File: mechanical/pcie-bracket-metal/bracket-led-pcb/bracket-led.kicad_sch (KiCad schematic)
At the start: 5 parts, among them J1 SM08B-SURS-TF(LF)(SN)

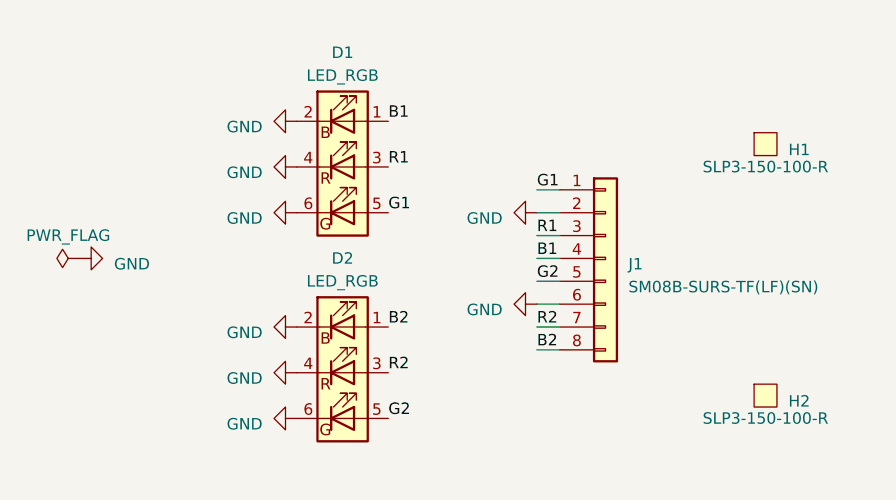
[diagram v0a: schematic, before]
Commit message: Update LED panel design after review
- Reduce size to fit in current allowed volume
- Move connector for improved strain relief
- Match RGB pinout on fmc host
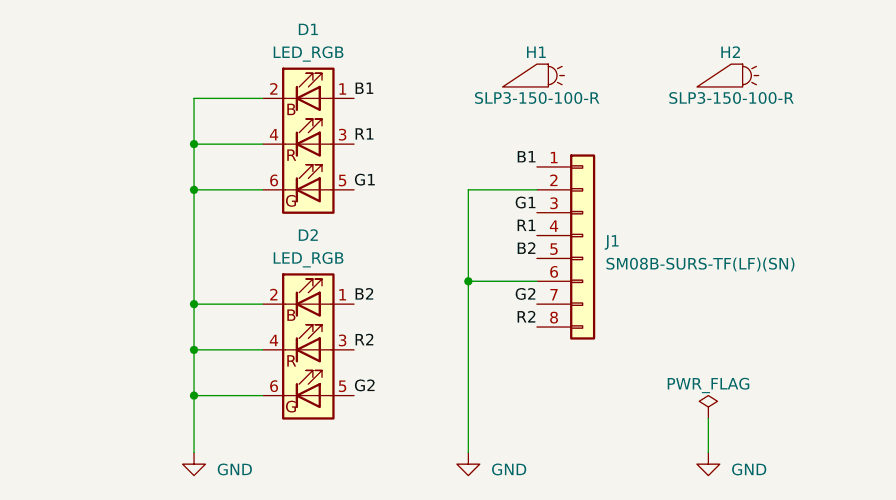
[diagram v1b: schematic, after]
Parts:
- H1: renamed from H2; symbol Open Ephys:SLP3-150-100-R -> jonnew:LIGHTPIPE
- H2: renamed from H1; symbol Open Ephys:SLP3-150-100-R -> jonnew:LIGHTPIPE
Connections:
- net B1: now also J1.1 (Pin_1); no longer J1.4 (Pin_4)
- net B2: now also J1.5 (Pin_5); no longer J1.8 (Pin_8)
- net G1: now also J1.3 (Pin_3); no longer J1.1 (Pin_1)
- net G2: now also J1.7 (Pin_7); no longer J1.5 (Pin_5)
- net R1: now also J1.4 (Pin_4); no longer J1.3 (Pin_3)
- net R2: now also J1.8 (Pin_8); no longer J1.7 (Pin_7)
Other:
- moved on the sheet: D1, D2, J1
